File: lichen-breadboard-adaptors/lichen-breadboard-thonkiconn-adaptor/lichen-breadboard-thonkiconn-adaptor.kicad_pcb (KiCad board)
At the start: 2 copper layers, 11 x 22 mm, 3 parts, among them J1 Thonkiconn_Mono_Audio_Jack, J2 Conn_01x03_Pin, J3 Conn_01x03_Pin

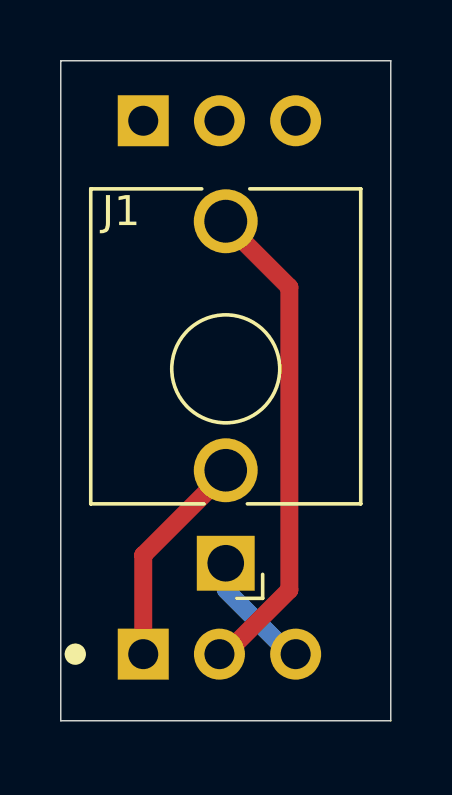
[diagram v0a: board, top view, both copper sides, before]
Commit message: Updates Lichen symbols and footprints. Fixes to Crustose and Vactrol VCA. Adds 3D model of the RP2350 dual USB board.
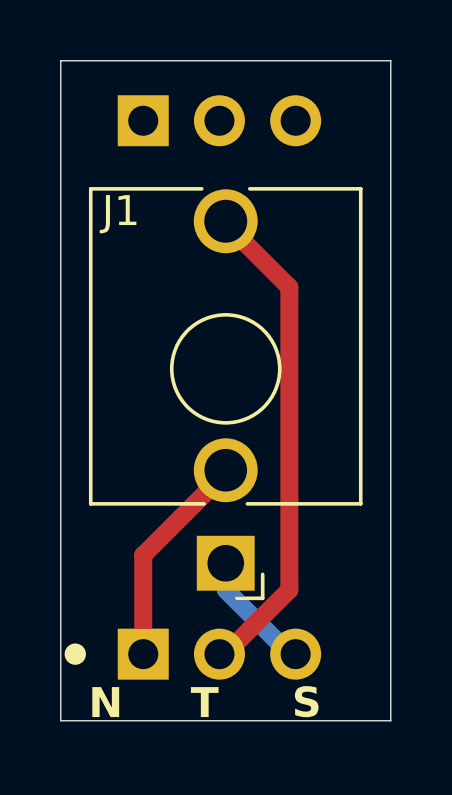
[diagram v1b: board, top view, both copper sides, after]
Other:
- board text added: "N"
- board text added: "S"
- board text added: "T"
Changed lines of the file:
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@@
 		(layer "Edge.Cuts")
+	)
+	(gr_text "N"
+		(at 101.5 122 0)
+		(layer "F.SilkS")
+		(effects
+			(font
+				(size 1 1)
+				(thickness 0.2)
+				(bold yes)
+			)
+			(justify bottom)
+		)
+	)
+	(gr_text "T"
+		(at 104.8 122 0)
+		(layer "F.SilkS")
+		(effects
+			(font
+				(size 1 1)
+				(thickness 0.2)
+				(bold yes)
+			)
+			(justify bottom)
+		)
+	)
+	(gr_text "S"
+		(at 108.2 121.4 0)
+		(layer "F.SilkS")
+		(effects
+			(font
+				(size 1 1)
+				(thickness 0.2)
+				(bold yes)
+			)
+		)
 	)
 	(gr_text "Jack Adaptor\nv1 Nov. 2025"
